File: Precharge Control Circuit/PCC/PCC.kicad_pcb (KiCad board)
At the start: 2 copper layers, 123.5 x 151.7 mm, 167 parts, among them J1 Conn_01x04_Socket, J10 INVTR, J11 AMP BYP, J12 AMP BYP, J13 462070206, J2 874271202, J3 462070206, J4 Conn_02x14_Counter_Clockwise, J5 IMD, J6 Thermistor Expansion, J8 BMS, J9 EnergyMeter, K1 Relay_SPDT, Q1 IRLZ44N, Q2 IRLZ44N, Q3 Q_NMOS_GSD, Q4 Q_NMOS_GSD, Q5 Q_NMOS_GSD, U1 SN65HVD230, U10 4N35, U11 LM555xN, U2 4N35, U3 4N35, U7 TLV2372IP, U8 LM1117T-5.0, U9 TLV2372IP

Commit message: PCC finalized
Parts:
- removed DEBUG_1: LED, LED_THT:LED_D5.0mm
- removed F13, F14, F15, F16, F17, F18, F2: 1A, footprints:5x20fuseblock
- removed H4: MountingHole_Pad, MountingHole:MountingHole_3.2mm_M3_DIN965_Pad_TopBottom
- removed R12, R5, R7, R8: 3k, Resistor_SMD:R_2512_6332Metric
- removed R13, R14, R17, R18, R19, R78, R79, R80: 0.43R 1/2W, Resistor_SMD:R_0805_2012Metric_Pad1.20x1.40mm_HandSolder
- removed R64, R66, R68: 20k, Resistor_SMD:R_0805_2012Metric
- removed R74: 22k, Resistor_SMD:R_0805_2012Metric
- removed R76: 11k, Resistor_SMD:R_0805_2012Metric
- removed R77: 10k, Resistor_SMD:R_0805_2012Metric
- removed R_pullup1: 15k, Resistor_SMD:R_0805_2012Metric
- added F20: 1A, footprints:5x20fuseblock, F.Cu at (147.6, 21.2)
- added F21: 1A, footprints:5x20fuseblock, B.Cu at (149.4, 78.2)
- added F22: 1A, footprints:5x20fuseblock, B.Cu at (162.4, 45.0)
- added F23: 1A, footprints:5x20fuseblock, F.Cu at (149.3, 78.2)
- added F24: 1A, footprints:5x20fuseblock, B.Cu at (147.6, 21.2)
- added F25: 1A, footprints:5x20fuseblock, B.Cu at (144.6, 105.9)
- added F26: 1A, footprints:5x20fuseblock, F.Cu at (144.6, 106.0)
- added HS3: Heatsink_Pad, footprints:smolsink, F.Cu at (137.2, 155.0)
- added HS4: Heatsink_Pad, footprints:smolsink, F.Cu at (139.5, 141.6)
- added R82: 0.3r, Resistor_SMD:R_2512_6332Metric_Pad1.40x3.35mm_HandSolder, B.Cu at (150.3, 118.7)
- C1, C18, C2, C20, C24, C25, C26, C27, C3, C4, C5, C6, C7, C8, R20, R21, R22, R23, R24, R26, R27, R28, R30, R31, R32, R35, R36, R37, R38, R41, R42, R43, R44, R45, R46, R48, R61, R62, R63, R65, R67, R69, R70: moved to B.Cu
- F3, F4: value 1A -> 1.25; moved to B.Cu
- J2: footprint footprints:12pRminifit -> footprints:12pSTminifit
- K1: value Relay_SPDT -> RinconRH3; footprint footprints:Precharge_Discharge_Relay_Rincon -> footprints:RH3_Mount
- R1, R2: value 3k -> R_US; footprint Resistor_SMD:R_2512_6332Metric -> footprints:TO-220-2_Vertical-SMD; moved to F.Cu
- R10, R11, R9: value 3k -> 10k; footprint Resistor_SMD:R_2512_6332Metric -> Resistor_SMD:R_0805_2012Metric
- R15, R16: value 0.43R 1/2W -> 20k; footprint Resistor_SMD:R_0805_2012Metric_Pad1.20x1.40mm_HandSolder -> Resistor_SMD:R_0805_2012Metric
- R4: value 3k -> 22k; footprint Resistor_SMD:R_2512_6332Metric -> Resistor_SMD:R_0805_2012Metric
- R81: value 0.43R 1/2W -> 0.3r; footprint Resistor_SMD:R_0805_2012Metric_Pad1.20x1.40mm_HandSolder -> Resistor_SMD:R_2512_6332Metric_Pad1.40x3.35mm_HandSolder; moved to B.Cu
- moved R9 88.3 mm to (67.6, 122.0), turned to 0 degrees
- moved R16 83.0 mm to (119.2, 122.3), turned to 0 degrees
- moved R10 68.7 mm to (110.1, 101.8), turned to 0 degrees
- moved R4 66.9 mm to (81.8, 122.3), turned to -90 degrees
- moved R15 63.3 mm to (119.3, 119.0), turned to 180 degrees
- moved R11 45.8 mm to (115.8, 107.6), turned to 180 degrees
- moved C27 33.4 mm to (116.5, 111.8), turned to 180 degrees
- moved R61 25.7 mm to (114.8, 123.2)
- moved R62 20.2 mm to (116.3, 115.9), turned to 90 degrees
- moved R1 17.2 mm to (142.1, 146.9), turned to 180 degrees
- moved R2 14.8 mm to (139.7, 160.6), turned to 180 degrees
- moved F3 14.4 mm to (142.1, 139.3), turned to 45 degrees
- moved C30 13.3 mm to (78.8, 121.4)
- moved R63 10.6 mm to (121.2, 126.5), turned to 180 degrees
- moved R81 10.4 mm to (154.2, 152.7), turned to 90 degrees
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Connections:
- C31 pad 2: +12 ISO -> 12V_UNISO
- C32 pad 2: +12 ISO -> 12V_UNISO
- F1 pad 2: Net-(F1-Pad2) -> /FusedTS+ (EM)
- F19 pad 2: Net-(F19-Pad2) -> /FusedTS + (indicator)
- J13 pad 3: GND ISO -> TS- unfused
- J13 pad 6: TS- unfused -> GND ISO
- Q3 pad 1: Net-(DEBUG_1-K) -> Net-(Q3-G)
- R1 pad 1: TS+ unfused -> /TSMP+
- R1 pad 2: Net-(R1-Pad2) -> TS+ unfused
- R10 pad 1: Net-(R10-Pad1) -> 12V_UNISO
- R10 pad 2: Net-(R10-Pad2) -> V_BIAS
- R11 pad 1: Net-(R11-Pad1) -> 12V_UNISO
- R11 pad 2: /TSMP+ -> Net-(Q3-G)
- R15 pad 1: Net-(F15-Pad2) -> Net-(R15-Pad1)
- R15 pad 2: /FusedTS + (expansion) -> Net-(R15-Pad2)
- R16 pad 1: Net-(F16-Pad2) -> V_SNS
- R16 pad 2: /FusedTS - (IMD) -> Net-(R15-Pad1)
- R2 pad 1: TS- unfused -> /TSMP-
- R2 pad 2: Net-(R2-Pad2) -> TS- unfused
- R4 pad 1: Net-(R1-Pad2) -> GLV+
- R4 pad 2: Net-(R4-Pad2) -> Net-(U11-DIS)
- R62 pad 1: Net-(R62-Pad1) -> Net-(R15-Pad2)
- R9 pad 1: Net-(R7-Pad2) -> GLV+
- R9 pad 2: Net-(R11-Pad1) -> RTM_SIG
- U12 pad 6: +12 ISO -> 12V_UNISO
- U9 pad 1: Net-(DEBUG_1-K) -> Net-(Q3-G)
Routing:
- net TS-: track 0.00 -> 158.0 mm, vias 0 -> 14
- net /TSMP-: track 0.00 -> 146.5 mm
- net /TSMP+: track 0.00 -> 124.1 mm
- net GND ISO: track 0.00 -> 122.7 mm, vias 0 -> 100
- net Vin_Accu: track 0.00 -> 86.3 mm, vias 0 -> 1
- net TS+: track 0.00 -> 73.4 mm, vias 0 -> 18
- net Net-(R3-Pad1): track 0.00 -> 58.0 mm
- net GLV+: track 299.1 -> 343.4 mm, vias 0 -> 2
- net 12V_UNISO: track 0.00 -> 39.9 mm, vias 0 -> 6
- net RTM_SIG: track 43.3 -> 70.6 mm, vias 1 -> 2
- net HighVoltage-: track 0.00 -> 24.8 mm, vias 0 -> 27
- net /FusedTS - (indicator): track 0.00 -> 24.8 mm
- net /FusedTS + (expansion): track 0.00 -> 22.2 mm
- net /FusedTS - (expansion): track 0.00 -> 20.4 mm
- net /FusedTS+ (EM): track 0.00 -> 18.5 mm
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- added copper zone on F.Cu, net GND ISO
- added copper zone on B.Cu, net HighVoltage-
- added copper zone on F.Cu, net HighVoltage-
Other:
- outline, holes or cut-outs redrawn
- board text added: "0ADKC1000-BE ONLY!"
- board text added: "0ADKC1250-BE ONLY"
- board text added: "B+"
- board text added: "B-"
- board text added: "Battery Board By Gabriel Schoene"
- board text added: "DCDC +"
- board text added: "DCDC-"
- board text added: "EM +"
- board text added: "IMD +"
- board text added: "IMD -"
- board text added: "INDICATOR +"
- board text added: "INDICATOR -"
- board text added: "TS+"
- board text added: "TS-"
- board text added: "TSMP+"
- board text added: "TSMP-"
- board text added: "dont forget to remove middle 2 pins and key hsng"
- board text removed: "12v"
- board text removed: "DCDC Enable"
- board text removed: "DNP"
- board text removed: "NOTE RTML and other 4 pins are NOT interchangable!!"
- board text removed: "sig"
- board text removed: "sorry about this hole's dimensions :("

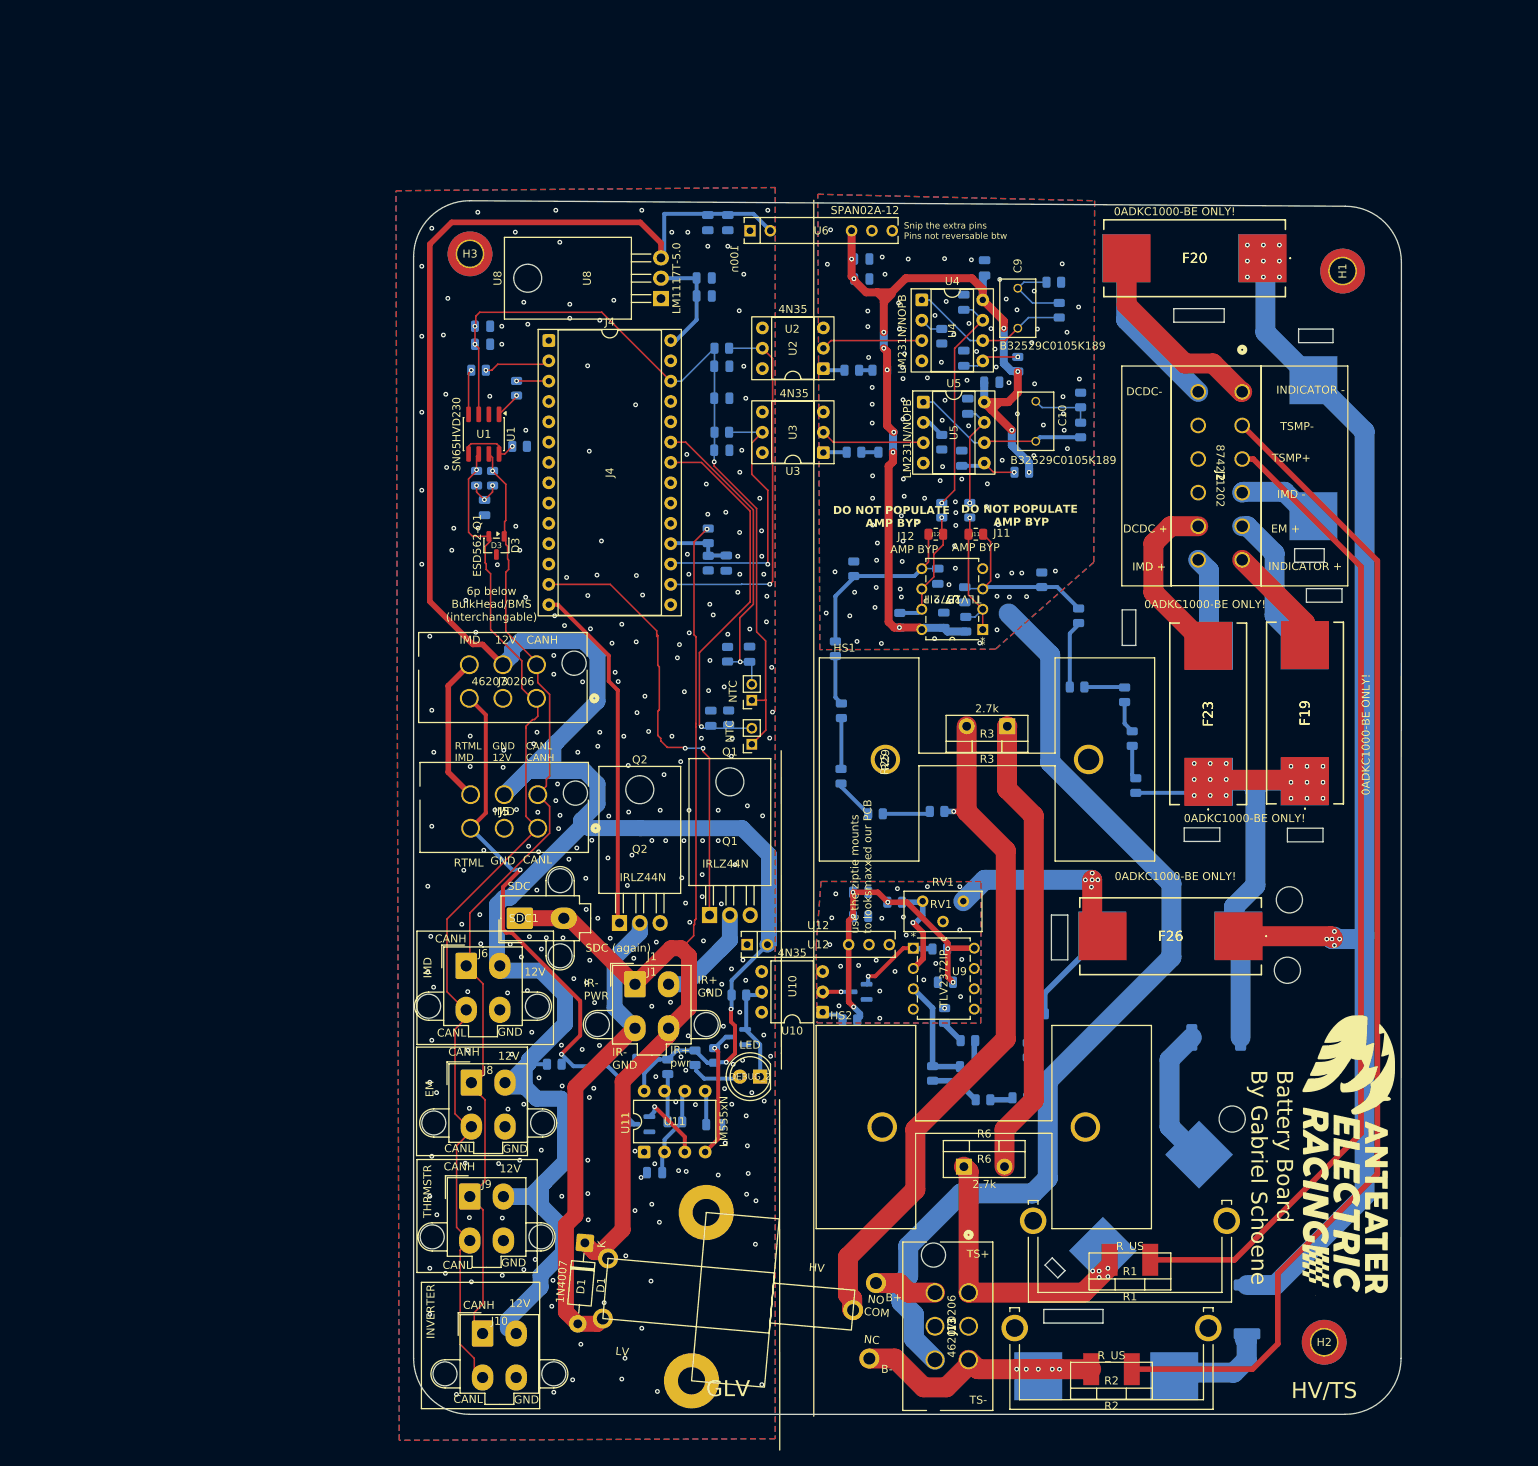
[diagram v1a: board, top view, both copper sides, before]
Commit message: PCC was rolled back rerolled it
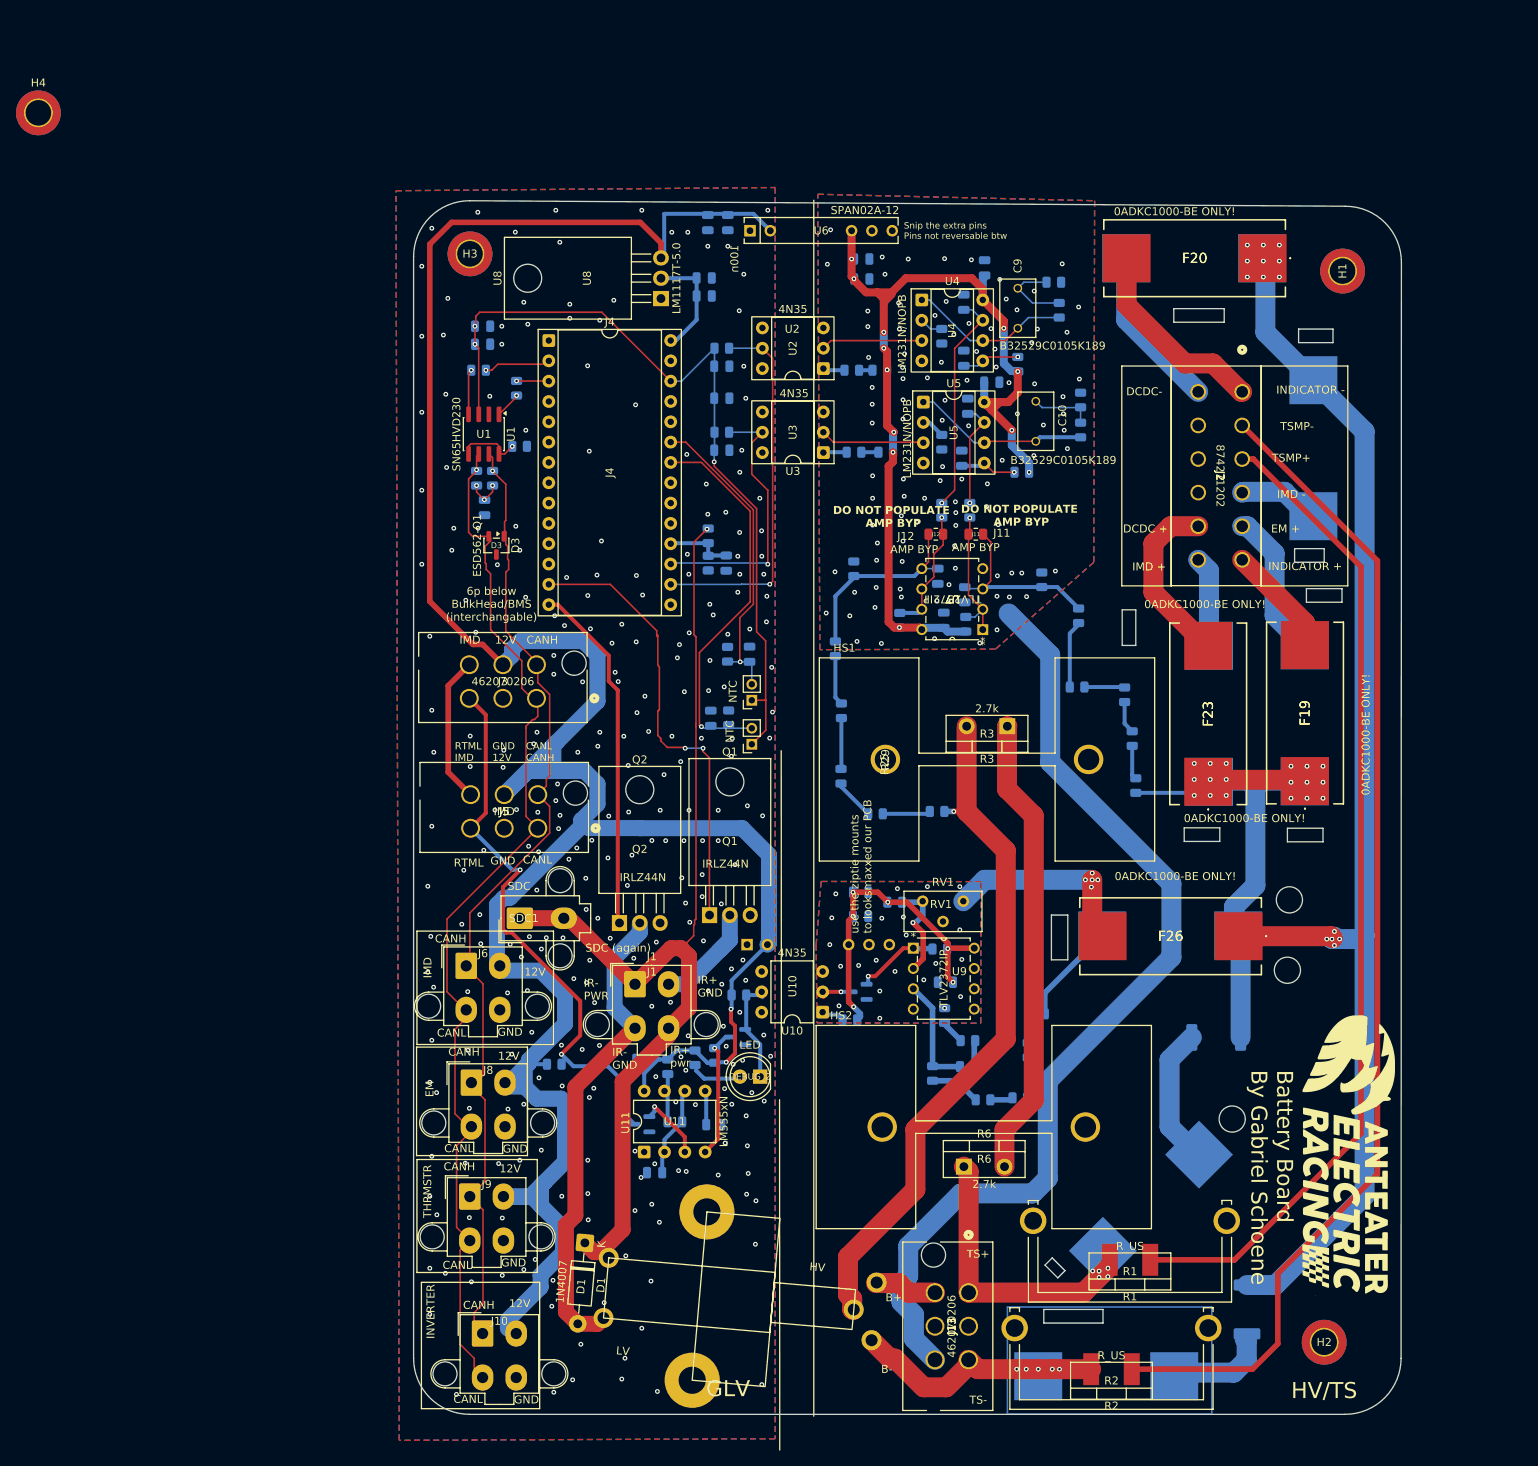
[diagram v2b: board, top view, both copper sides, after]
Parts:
- added H4: MountingHole_Pad, MountingHole:MountingHole_3.2mm_M3_DIN965_Pad_TopBottom, F.Cu at (3.08, 3.08)
- K1: value RinconRH3 -> Relay_SPDT
- U12: moved to B.Cu
- moved K1 0.11 mm to (94.8, 151.8)
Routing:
- net TS- unfused: track 31.5 -> 32.2 mm
